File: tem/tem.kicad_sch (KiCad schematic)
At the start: 55 parts, among them J13 Conn_01x05_Pin, J14 Conn_01x02_Pin, J15 Conn_01x02_Pin, J16 Conn_01x02_Pin, J17 Conn_01x02_Pin, U2 MAX3051ESA+, U3 AZ1117CH-3.3TRG1, U4 MAX14878

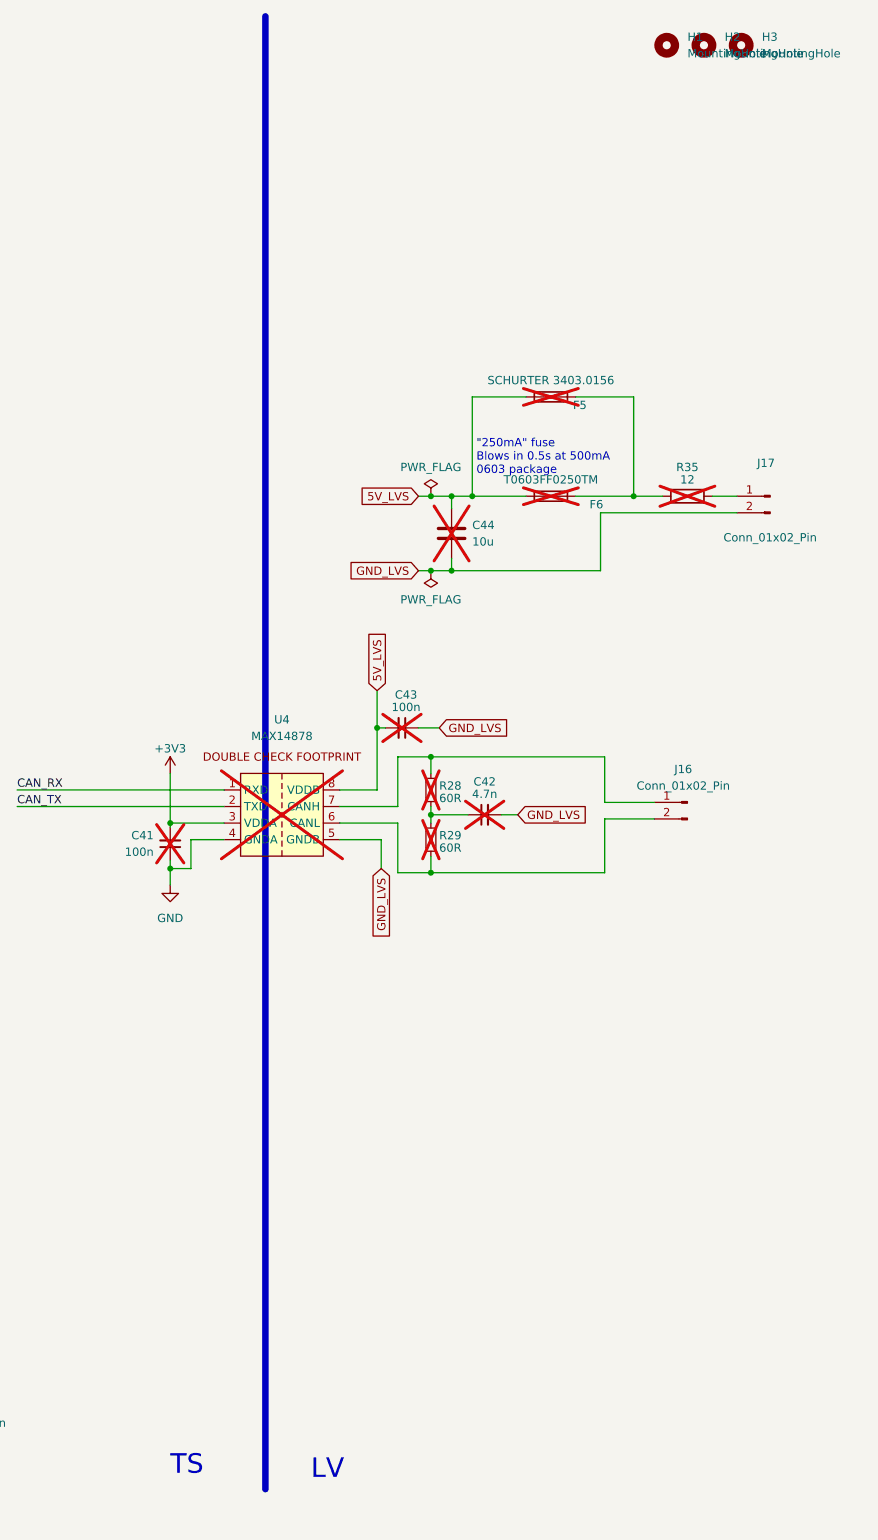
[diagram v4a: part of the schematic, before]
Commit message: Positioned thermistor connectors
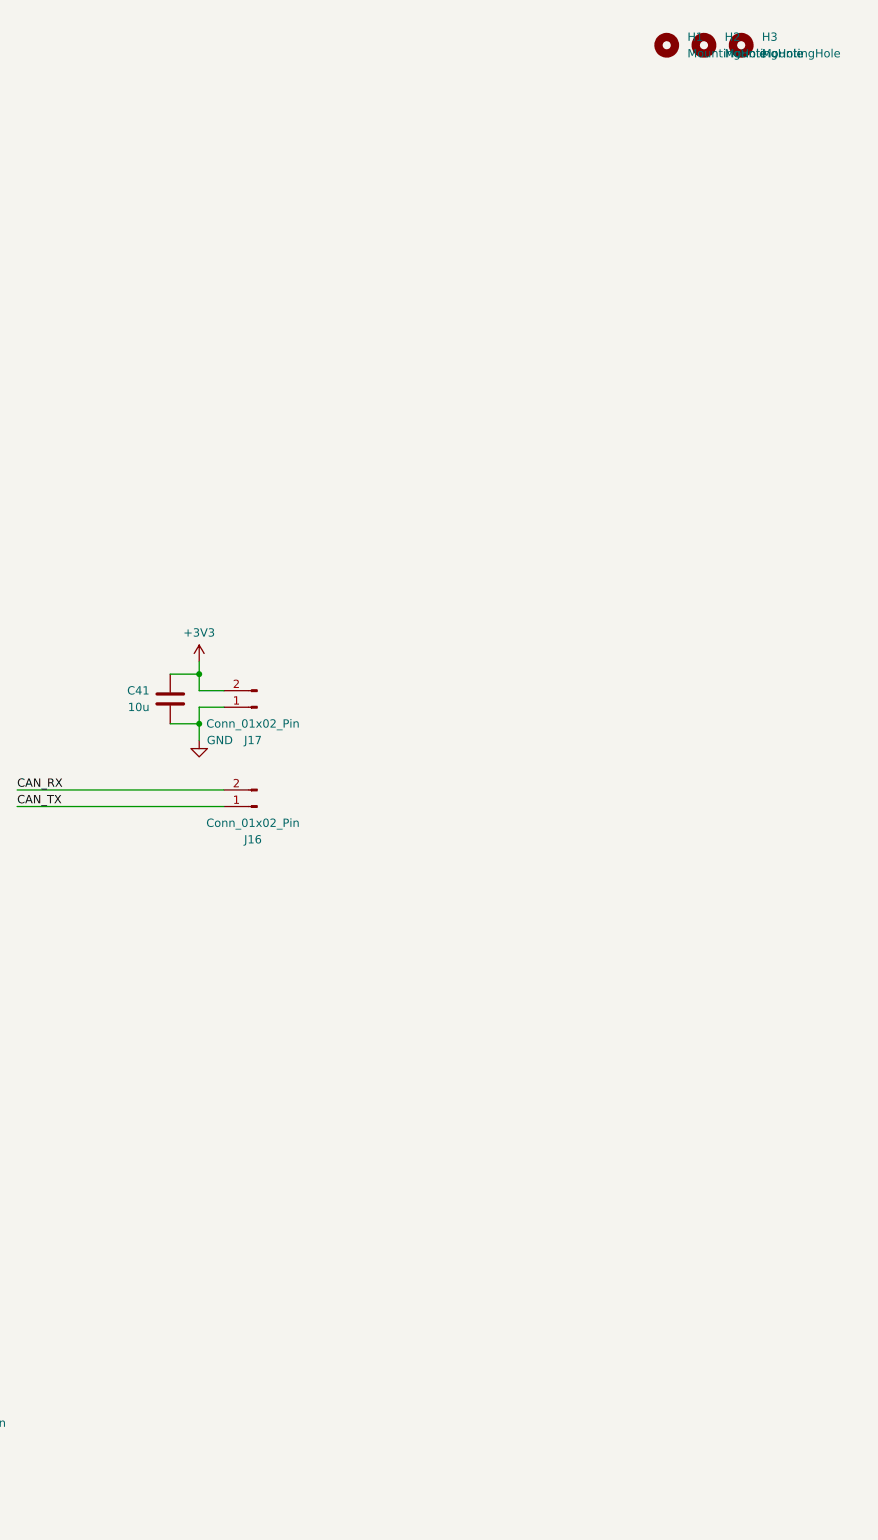
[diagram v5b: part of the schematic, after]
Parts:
- removed C41, C43: 100n, Capacitor_SMD:C_0805_2012Metric_Pad1.18x1.45mm_HandSolder, symbol Device:C_Small
- removed C42: 4.7n, Capacitor_SMD:C_0805_2012Metric_Pad1.18x1.45mm_HandSolder, symbol Device:C_Small
- removed C44: 10u, Capacitor_SMD:C_0805_2012Metric_Pad1.18x1.45mm_HandSolder, symbol Device:C
- removed F5: SCHURTER 3403.0156, Fuse:Fuse_Schurter_UMT250, symbol Device:Fuse
- removed F6: T0603FF0250TM, Fuse:Fuse_0603_1608Metric_Pad1.05x0.95mm_HandSolder, symbol Device:Fuse
- removed R28, R29: 60R, Resistor_SMD:R_0805_2012Metric_Pad1.20x1.40mm_HandSolder, symbol Device:R_Small
- removed R35: 12, Resistor_SMD:R_0805_2012Metric_Pad1.20x1.40mm_HandSolder, symbol Device:R
- removed U4: MAX14878, Package_SO:SOIC-8W_5.3x5.3mm_P1.27mm, symbol SUFST:MAX14878
- added C41: 10u, Capacitor_SMD:C_0805_2012Metric_Pad1.18x1.45mm_HandSolder, symbol Device:C
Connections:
- net GND_LVS is gone; now on net +3V3: J17.2 (Pin_2)
- net +3V3: now also C41.1
- net CAN_RX: now also J16.2 (Pin_2)
- net CAN_TX: now also J16.1 (Pin_1)
- net GND: now also J17.1 (Pin_1), C41.2
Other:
- note removed: "LV"
- note removed: "TS"

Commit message: More reshuffling, increased pad sizes
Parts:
- J14, J15, J16, J17: footprint sufst-lib:Conn2_DoubleHole -> sufst-lib:Conn2_SMD
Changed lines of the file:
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@@
       (effects (font (size 1.27 1.27)))
     )
-    (property "Footprint" "sufst-lib:Conn2_DoubleHole" (at 25.4 43.815 0)
+    (property "Footprint" "sufst-lib:Conn2_SMD" (at 25.4 43.815 0)
       (effects (font (size 1.27 1.27)) hide)
     )
@@
       (effects (font (size 1.27 1.27)))
     )
-    (property "Footprint" "sufst-lib:Conn2_DoubleHole" (at 317.5 123.19 0)
+    (property "Footprint" "sufst-lib:Conn2_SMD" (at 317.5 123.19 0)
       (effects (font (size 1.27 1.27)) hide)
     )
@@
       (effects (font (size 1.27 1.27)))
     )
-    (property "Footprint" "sufst-lib:Conn2_DoubleHole" (at 317.5 138.43 0)
+    (property "Footprint" "sufst-lib:Conn2_SMD" (at 317.5 138.43 0)
       (effects (font (size 1.27 1.27)) hide)
     )
@@
       (effects (font (size 1.27 1.27)))
     )
-    (property "Footprint" "sufst-lib:Conn2_DoubleHole" (at 272.415 230.505 0)
-      (effects (font (size 1.27 1.27)) hide)
-    )
+    (property "Footprint" "sufst-lib:Conn2_SMD" (at 272.415 230.505 0)
+      (effects (font (size 1.27 1.27)) hide)
+    )

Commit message: Initial layout done
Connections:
- net at R25.2, U2.7 (CANH): now also J14.1 (Pin_1); no longer J14.2 (Pin_2)
- net at R26.1, U2.6 (CANL): now also J14.2 (Pin_2); no longer J14.1 (Pin_1)
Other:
- moved on the sheet: J14
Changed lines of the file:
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@@
     )
   )
-  (symbol (lib_id "Connector:Conn_01x02_Pin") (at 272.415 230.505 180) (unit 1)
+  (symbol (lib_id "Connector:Conn_01x02_Pin") (at 272.415 227.965 0) (mirror y) (unit 1)
     (in_bom yes) (on_board yes) (dnp no)
-    (property "Reference" "J14" (at 271.78 235.585 0)
+    (property "Reference" "J14" (at 271.78 222.885 0)
       (effects (font (size 1.27 1.27)))
     )
-    (property "Value" "Conn_01x02_Pin" (at 271.78 233.045 0)
+    (property "Value" "Conn_01x02_Pin" (at 271.78 225.425 0)
       (effects (font (size 1.27 1.27)))
     )
-    (property "Footprint" "sufst-lib:Conn2_SMD" (at 272.415 230.505 0)
+    (property "Footprint" "sufst-lib:Conn2_SMD" (at 272.415 227.965 0)
       (effects (font (size 1.27 1.27)) hide)
     )
-    (property "Datasheet" "~" (at 272.415 230.505 0)
+    (property "Datasheet" "~" (at 272.415 227.965 0)
       (effects (font (size 1.27 1.27)) hide)
     )

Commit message: Tweaks
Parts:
- U1: value ~ -> PIC18F47Q84-I/PT
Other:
- note added: "Fuse not stocked at Mouser Replacement: F0603E0R25FSTR\INT"
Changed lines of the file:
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@@
+    (stroke (width 0) (type default))
+  )
+  (polyline (pts (xy 52.705 40.64) (xy 62.865 34.29))
     (stroke (width 0) (type default))
   )
@@
   (text "TODO:\n- Fuses on input, 3V3, VDD of CAN chip, MCU (and thermistor-VCC?)\n  (should be very low current, 20mA range). Fuses should be before\n  the decoupling caps.\n- Replace 100u capacitor with a lower profile one (or many ceramics\n  in parallel).\n- Decide on footprints for all connectors.\n\nAlso before we manufacture this:\n- Triple check MCU pins, CAN capabilities, ADC capabilities, SAH time,\n  SAH charge (sampling too often could discharge the 100n capacitor on\n  each thermistor input), debugging method (current plan: PicKit3).\n- Check that we can emulate the thermistor expansion module. We would\n  need a second USB-CAN device to plug into the TEM connectors on the\n  BMS.\n- Check thermistor resistance curve (I assumed 10k at room temp)."
     (at 25.4 191.135 0)
+    (effects (font (size 1.27 1.27)) (justify left bottom))
+  )
+  (text "Fuse not stocked at Mouser\nReplacement: F0603E0R25FSTR\\INT"
+    (at 57.785 34.29 0)
     (effects (font (size 1.27 1.27)) (justify left bottom))
   )
@@
       (effects (font (size 1.27 1.27)))
     )
-    (property "Value" "~" (at 158.115 114.935 0)
-      (effects (font (size 1.27 1.27)))
-    )
+    (property "Value" "PIC18F47Q84-I/PT" (at 139.065 175.895 0)
+      (effects (font (size 1.27 1.27)))
+    )
